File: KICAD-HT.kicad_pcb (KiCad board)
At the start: 2 copper layers, 90 x 80 mm, 112 parts, among them J1 HV80_IN, J2 NAPPE_FILAMENT_HT, Q1 IPD050N10N5, Q2 IPD050N10N5, Q3 BSS127I, Q4 MMBT2222, Q5 BSS127I, T1 MSD1514-103ME, U1 UCC27517, U10 ISO7710, U11 AMC0311R, U12 UCC24612, U13 SN74LVC1G08, U14 TSV791, U15 ATL431, U16 LMV7219, U17 SN74LVC1G132, U18 SN74LVC1G74, U19 ISO7710F, U3 ISO7710, U5 DPC817, U7 AMC0311R, U8 AMC0311R, U9 AMC0302R

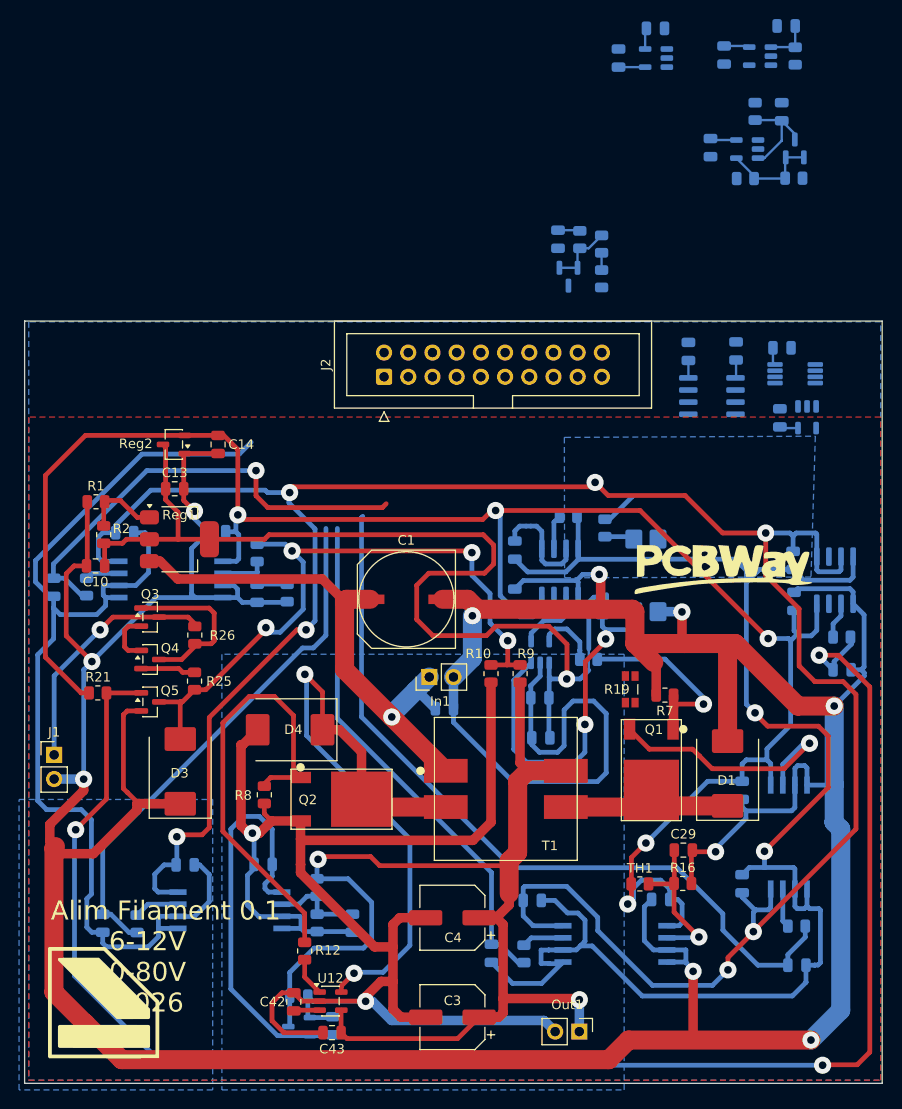
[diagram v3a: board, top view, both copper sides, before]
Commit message: Retouches manuelles : notation ~{} pour nPRE/nQ_TRIP, RAIL_8V25->RAIL_3V3_PRI, via 1.0/0.4mm
Renomme nPRE et nQ_TRIP en notation KiCad overline (~{PRE}/~{Q_TRIP}),
corrige une etiquette RAIL_8V25 en RAIL_3V3_PRI dans isolation.kicad_sch,
ajuste la taille de via par defaut (1.8/0.8 -> 1.0/0.4mm) et progresse sur
le placement/routage PCB.

Co-Authored-By: Claude Sonnet 5 <noreply@anthropic.com>
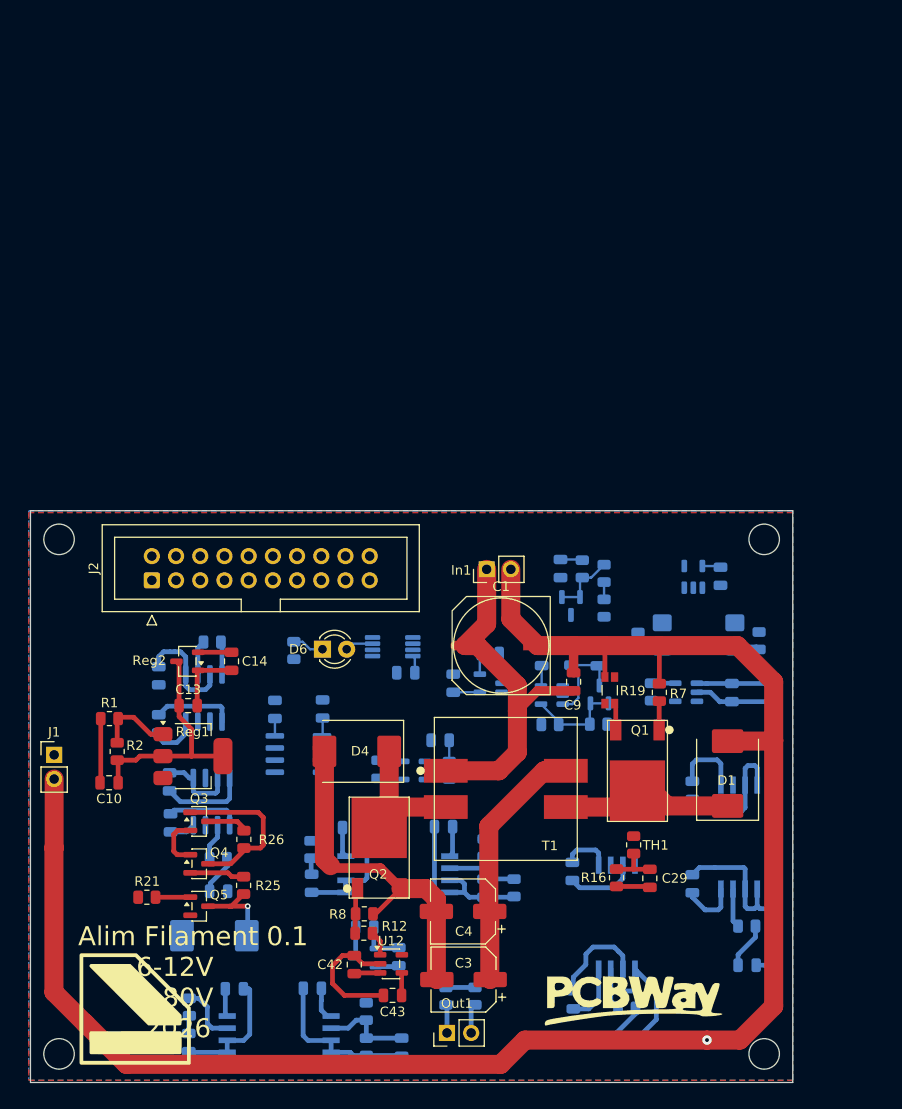
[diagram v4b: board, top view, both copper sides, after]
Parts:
- added ?: , , F.Cu at (76.0, 127.0)
- added ?: , , F.Cu at (150.0, 127.0)
- added ?: , , F.Cu at (150.0, 73.0)
- added D6: LED, LED_THT:LED_D3.0mm, F.Cu at (103.6, 84.5)
- added R34: 10k, Resistor_SMD:R_0805_2012Metric, B.Cu at (100.6, 84.7)
- added REF**: MountingHole_3.2mm_M3, MountingHole:MountingHole_3.2mm_M3, F.Cu at (76.0, 73.0)
- C9: moved to F.Cu
- D3, R10, R9: moved to B.Cu
- moved U17 83.3 mm to (113.3, 97.3)
- moved C51 83.3 mm to (109.5, 97.1)
- moved C52 83.3 mm to (116.0, 94.1)
- moved R33 83.3 mm to (117.0, 97.2)
- moved C34 69.4 mm to (87.6, 98.5)
- moved C36 69.4 mm to (92.8, 109.9)
- moved C35 69.4 mm to (87.7, 102.8)
- moved R20 69.4 mm to (92.7, 106.5)
- moved U10 69.4 mm to (92.0, 100.5)
- moved C54 67.9 mm to (121.2, 85.0)
- moved C50 67.9 mm to (117.4, 88.1)
- moved U16 67.9 mm to (121.3, 88.1)
- moved R28 60.9 mm to (127.5, 92.4)
- moved R29 60.9 mm to (132.6, 92.4)
- moved U14 60.9 mm to (127.7, 89.3)
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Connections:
- net nPRE renamed ~{PRE}
- R4 pad 1: RAIL_8V25 -> RAIL_3V3_PRI
- U18 pad 5: nQ_TRIP -> ~{Q_TRIP}
- U19 pad 2: nQ_TRIP -> ~{Q_TRIP}
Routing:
- net 3V3_ISO: track 264.4 -> 39.9 mm, vias 7 -> 0
- net GND: track 478.1 -> 269.7 mm, vias 10 -> 1
- net GND_CTRL: track 281.3 -> 86.1 mm, vias 2 -> 0
- net RAIL_3V3_PRI: track 220.6 -> 41.8 mm, vias 5 -> 0
- net VAR_GATE: track 174.8 -> 8.30 mm, vias 3 -> 0
- net VOUT_N: track 167.7 -> 75.2 mm, vias 2 -> 0
- net VOUT_P: track 124.2 -> 35.3 mm, vias 2 -> 0
- net RAIL_8V25: track 112.4 -> 32.6 mm, vias 1 -> 0
- net I_Shunt_ht: track 82.5 -> 4.86 mm
- net HV_BIAS: track 70.3 -> 12.4 mm, vias 4 -> 1
- net Vht: track 55.3 -> 1.89 mm
- net SW_SEC: track 69.0 -> 16.3 mm, vias 2 -> 0
- net Temp_ht: track 54.5 -> 4.20 mm
- net V_bias: track 48.4 -> 1.54 mm, vias 1 -> 0
- net GATE_Q2: track 47.1 -> 4.79 mm
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- removed copper zone on B.Cu, net GND_CTRL
- removed copper zone on B.Cu, net VOUT_N
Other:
- board size 90 x 80 mm -> 80 x 60 mm

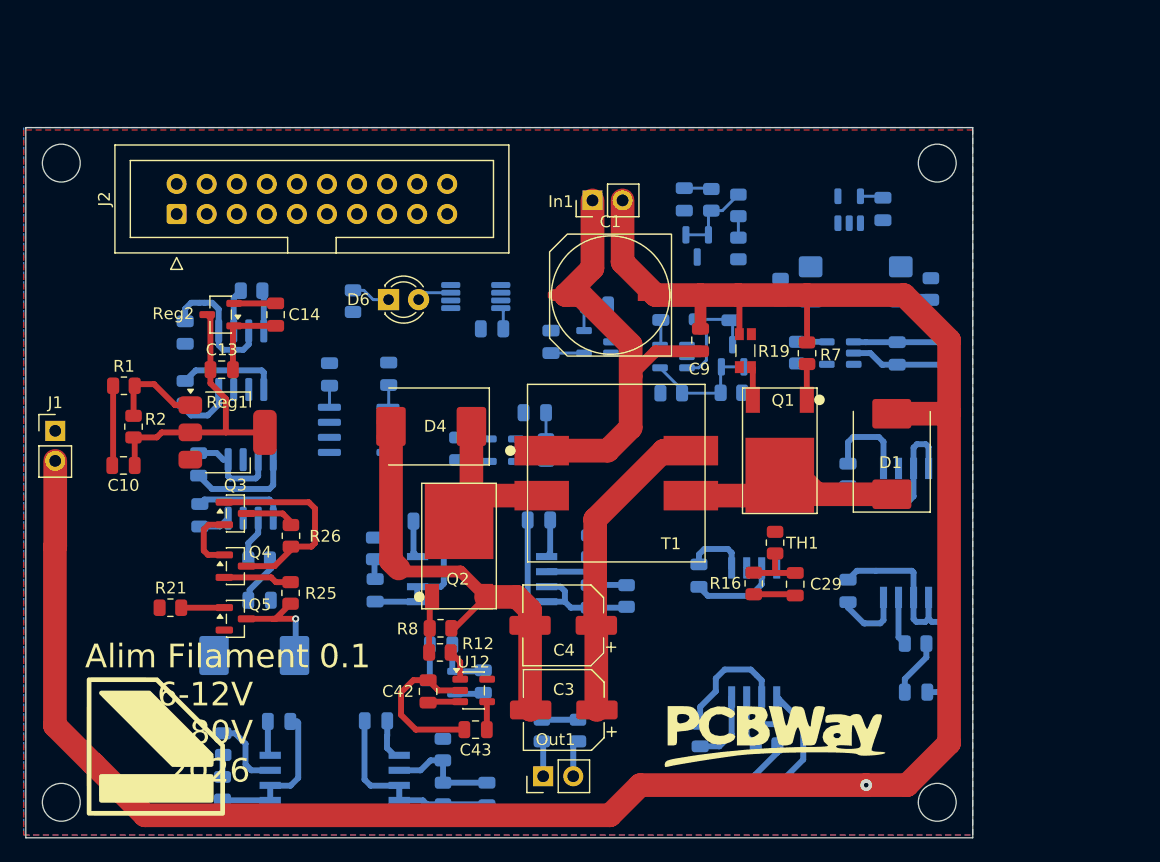
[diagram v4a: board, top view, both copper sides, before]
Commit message: Ajoute F1 (fusible VIN) et D2 (TVS RAIL_8V25), documente le plan d'isolation
Deux composants poses par l'utilisateur dans alim.kicad_sch pour fermer
les chemins 1 et 2 du confinement de defaut (doc/plan-isolation-4couches.md,
S8) : F1 en serie sur VIN, D2 (SMCJ10A) entre RAIL_8V25 et GND. Verifies
par calcul de position de broche (pas seulement par label) et par
rechargement standalone + hierarchie complete.

Nomenclature verifiee : D5/D6/D7/R30-R32 proposes par le plan
collisionnaient avec limitation-courant.kicad_sch (S19, posterieur au
commit de base du plan) -- corrige dans le plan, prochains reperes
libres D8/R35-R37. Documente dans S20 de 00-intention-conception.md.

Ignore aussi les exports BOM (KICAD-HT.txt/.xml), regeneres a chaque
passage, meme categorie que les rapports ERC/DRC.

Co-Authored-By: Claude Sonnet 5 <noreply@anthropic.com>
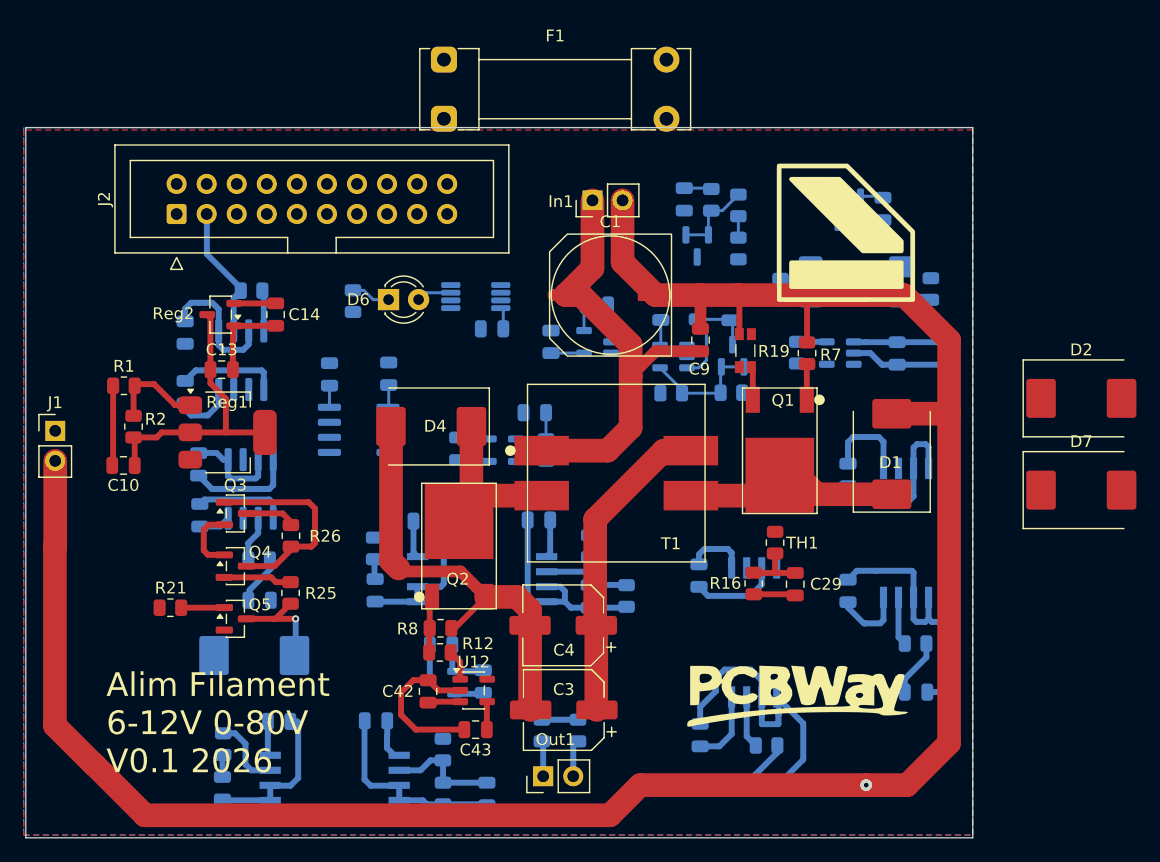
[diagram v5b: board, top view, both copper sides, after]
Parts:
- removed ? (x3): , 
- removed REF**: MountingHole_3.2mm_M3, MountingHole:MountingHole_3.2mm_M3
- added D2: SMCJ10A, Diode_SMD:D_SMC, F.Cu at (162.2, 92.9)
- added D7: SMCJ04A, Diode_SMD:D_SMC, F.Cu at (162.2, 100.6)
- added F1: Fuse, Fuse:Fuseholder_Clip-5x20mm_Littelfuse_111_Lateral_P18.80x5.00mm_D1.17mm_Horizontal, F.Cu at (108.3, 64.3)
- moved G*** 72.7 mm to (142.3, 78.9)
- moved G*** 3.89 mm to (138.5, 117.8)
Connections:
- In1 pad 1: VIN -> Net-(In1-Pin_1)
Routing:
- net PWM_ht: track 3.60 -> 11.3 mm
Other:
- board text added: "Alim Filament 6-12V 0-80V V0.1 2026"
- board text removed: "Alim Filament 0.1 6-12V 0-80V 2026"

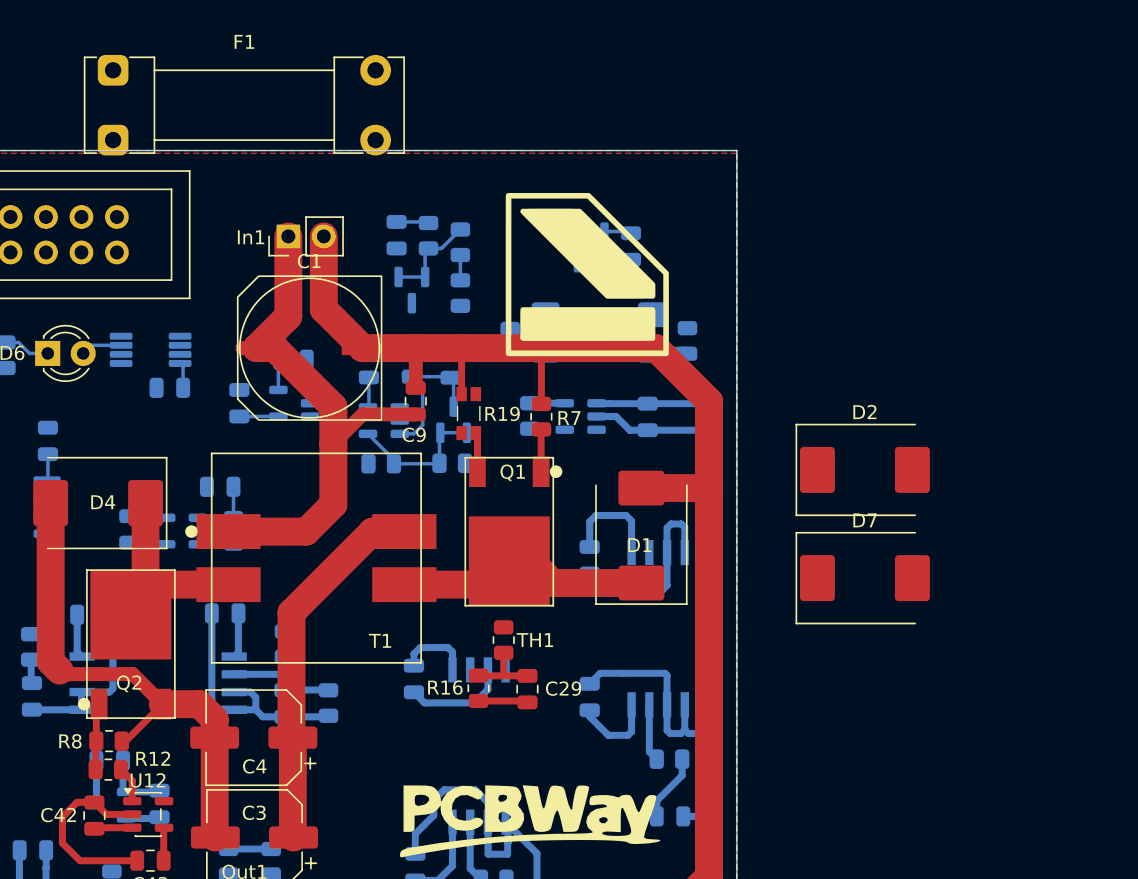
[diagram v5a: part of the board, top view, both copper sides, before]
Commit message: Resistances de reference inter-domaines (3x1M par barriere), F1 a 3A
Ajoute les trois chaines de resistances 1M en serie (R35/R6/R36,
R37/R38/R39, R42/R41/R40) qui ferment le point ouvert du plan
d'isolation (S3) : reference DC entre les trois domaines sans degrader
la CMTI. Chaine plutot qu'une resistance unique -- un seul 0805 n'a que
0,8mm d'ecart cuivre entre ses pastilles, loin des 8,5mm vises.

F1 fixe a 3A. TVS directe sur VIN retiree de la liste : deja presente
sur KICAD-C2000-powershield, en amont au niveau systeme.

Nomenclature reverifiee sur tout le projet, aucune collision. Fichiers
touches revalides (equilibre parentheses conscient des chaines,
chargement standalone + hierarchie complete). Documente au S20 de
00-intention-conception.md et dans doc/plan-isolation-4couches.md
(recommandation d'origine << resistance unique sous l'isolateur >>
corrigee).

Co-Authored-By: Claude Sonnet 5 <noreply@anthropic.com>
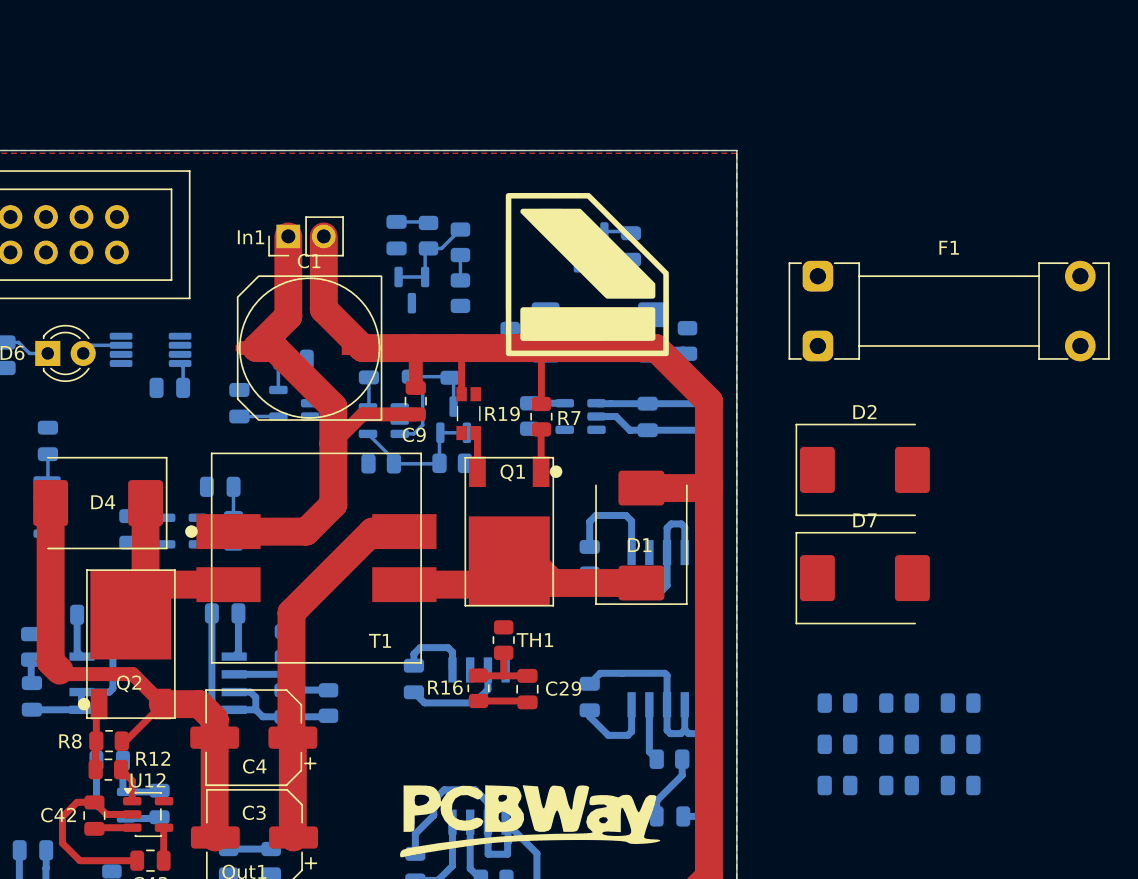
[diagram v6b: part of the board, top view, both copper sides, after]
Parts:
- added R35: 1M, Resistor_SMD:R_0805_2012Metric, B.Cu at (169.0, 112.5)
- added R36: 1M, Resistor_SMD:R_0805_2012Metric, B.Cu at (169.0, 115.5)
- added R37: 1M, Resistor_SMD:R_0805_2012Metric, B.Cu at (164.6, 109.6)
- added R38: 1M, Resistor_SMD:R_0805_2012Metric, B.Cu at (164.6, 112.5)
- added R39: 1M, Resistor_SMD:R_0805_2012Metric, B.Cu at (164.6, 115.5)
- added R40: 1M, Resistor_SMD:R_0805_2012Metric, B.Cu at (160.2, 109.6)
- added R41: 1M, Resistor_SMD:R_0805_2012Metric, B.Cu at (160.2, 112.5)
- added R42: 1M, Resistor_SMD:R_0805_2012Metric, B.Cu at (160.2, 115.5)
- added R6: 1M, Resistor_SMD:R_0805_2012Metric, B.Cu at (169.0, 109.6)
- moved F1 52.6 mm to (158.8, 79.0)
